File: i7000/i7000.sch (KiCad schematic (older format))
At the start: 53 parts, among them CN01 Conn_02x30_Counter_Clockwise, CN04 Conn_02x30_Counter_Clockwise, CN05 Conn_02x07_Counter_Clockwise

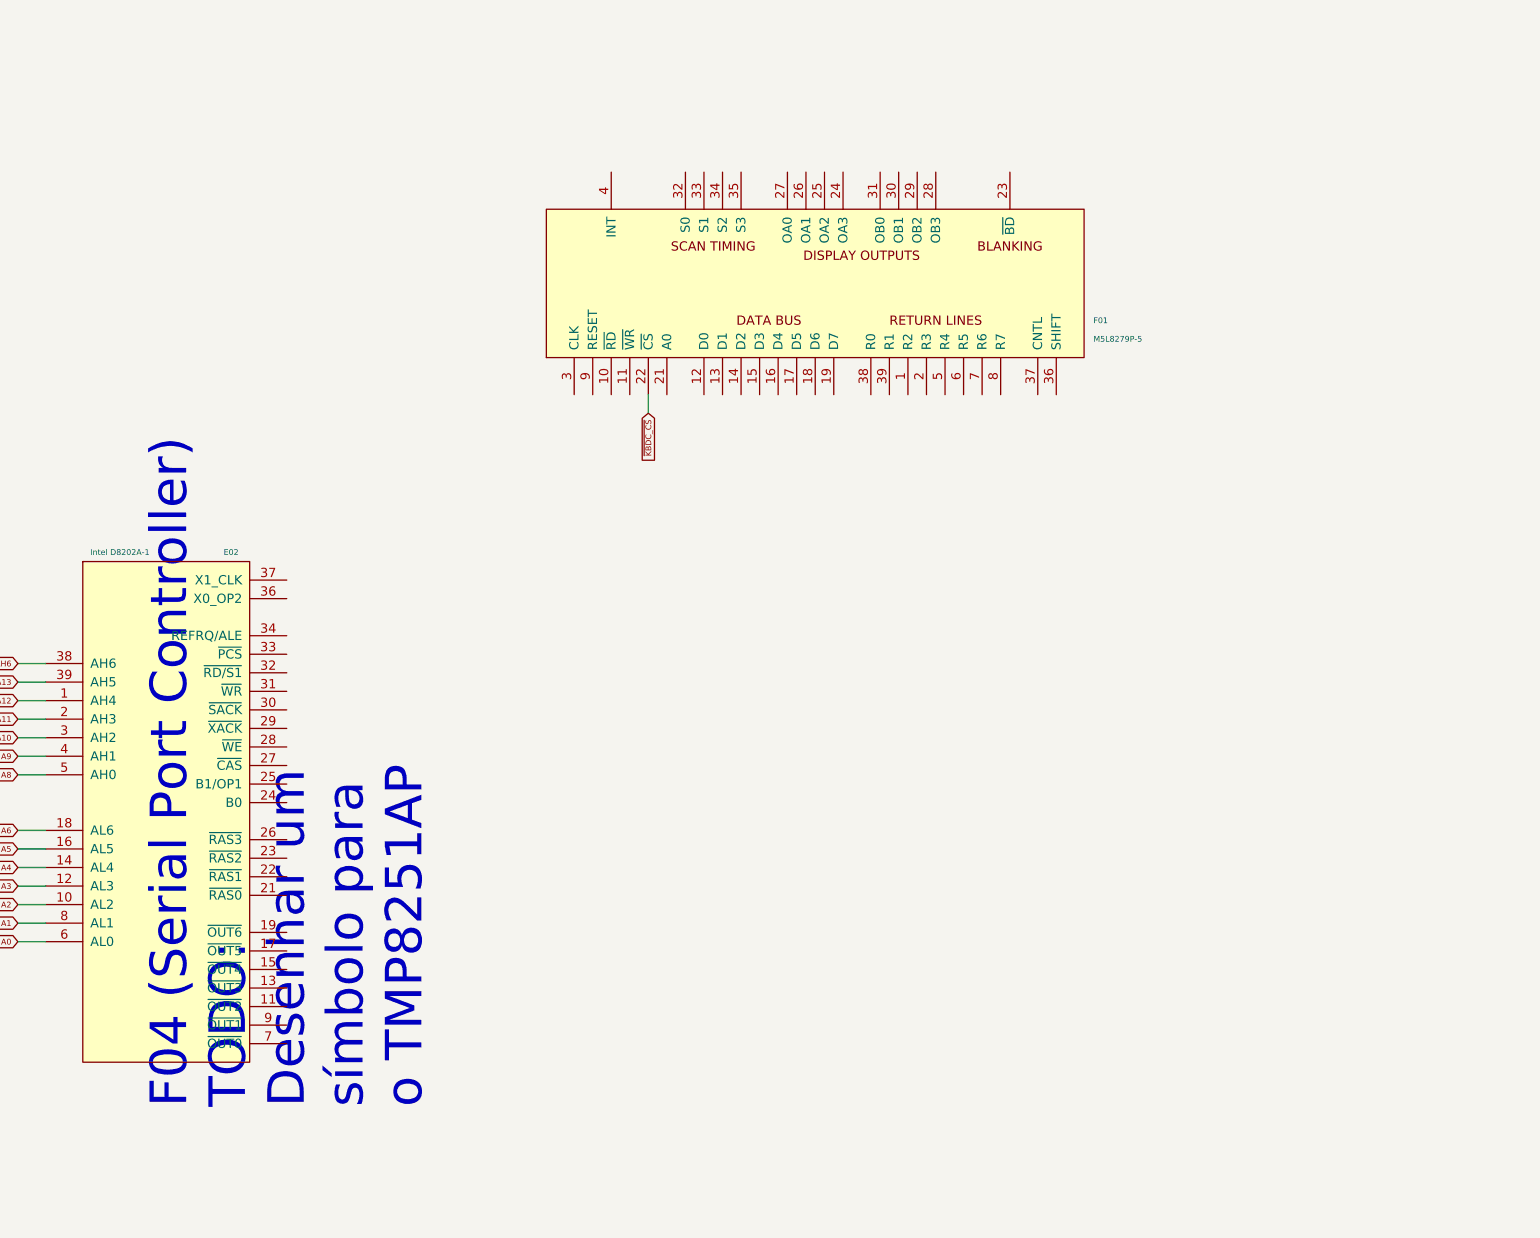
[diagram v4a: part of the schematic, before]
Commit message: TMP8251AP - Programmable Communication Interface (Serial Port Controller)
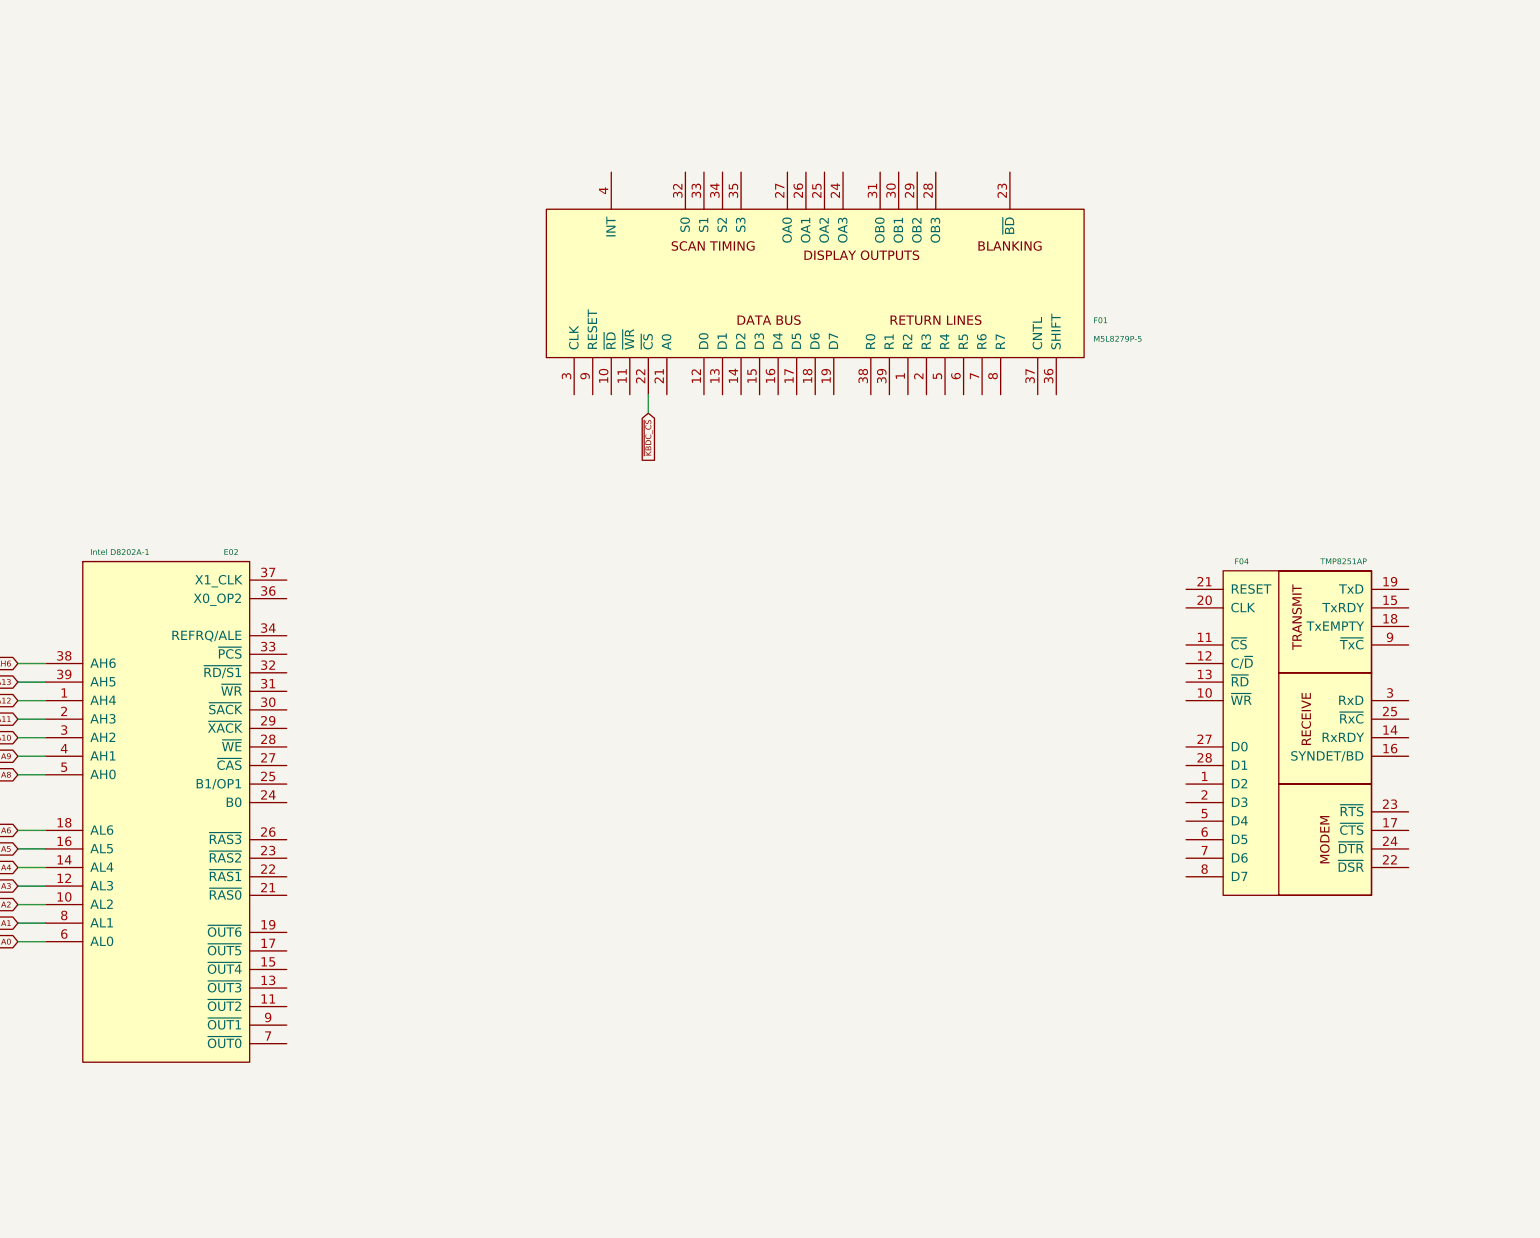
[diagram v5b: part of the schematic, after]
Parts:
- added F04: TMP8251AP, symbol chips_not_yet_available_on_kicad:TMP8251AP
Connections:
- net GND: now also F04.4 (GND)
- net VCC: now also F04.26 (VCC)
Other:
- note removed: "F04 (Serial Port Controller)\nTODO:\nDesenhar um\nsímbolo para\no TMP8251AP"
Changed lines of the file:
@@
 Wire Wire Line
 	25650 5150 25800 5150
-Text Notes 28200 12100 1    197  ~ 0
-F04 (Serial Port Controller)\nTODO:\nDesenhar um\nsímbolo para\no TMP8251AP
 Text GLabel 13600 6250 2    31   Output ~ 0
 ~I8251_CS
@@
 Wire Wire Line
 	29400 8350 29400 8250
+$Comp
+L chips_not_yet_available_on_kicad:TMP8251AP F04
+U 1 1 622E056F
+P 32850 10050
+F 0 "F04" H 32600 10950 31  0000 C CNN
+F 1 "TMP8251AP" H 33150 10950 31  0000 C CNN
+F 2 "" H 33100 10900 31  0001 C CNN
+F 3 "" H 33100 10900 31  0001 C CNN
+	1    32850 10050
+	1    0    0    -1
+$EndComp
 $EndSCHEMATC

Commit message: wip...
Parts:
- added CI03: WD2793A-PL2, symbol chips_not_yet_available_on_kicad:WD2793
- added CI07: 74LS240, symbol Logic_74xx:74LS240
- added CI18: 74LS373, symbol Logic_74xx:74LS373
- added unit 2 of CI19
- added CI20: 74LS14, symbol Logic_74xx:74LS14
- added unit 3 of CI21
- added E07: 74LS245, symbol Logic_74xx:74LS245
- added U?: 8259A, DIP-28, symbol intel:8259A
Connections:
- net A13: now also CI12.2 (A0)
- net A2: now also F07.1 (A0)
- net A3: now also F07.2 (A1)
- net A4: now also F07.3 (A2)
- net CN04_54: now also CN04.54 (Pin_54), E13.7 (O7)
- net GND: now also CI12.3 (A1), CI17.1 (OEa), CI17.10 (GND), CI17.19 (OEb)
- net VCC: now also CI17.20 (VCC)
- net ~FDC_CS: now also CI03.3 (~CS)
- net ~PIC_CS: now reaches F07.10 (O5)
- net ~PIC_CS: now also U?.1 (~CS~)
- net at F07.4 (E1): now also F07.5 (E2)
- net at F07.6 (E3): now also F15.3
- net ~A5: now reaches E28.12, F14.3, F15.2
- net CN04_10: now reaches CN04.10 (Pin_10)
- net CN04_10: now also CN01.10 (Pin_10), E13.14 (O1)
- net IR3: now reaches CN04.25 (Pin_25)
- net IR3: now also CI17.14 (O2a), CN01.25 (Pin_25), U?.21 (IR3)
- net CN04_52: now reaches CN04.52 (Pin_52)
- net CN04_52: now also CN01.52 (Pin_52), E13.13 (O2)
- net CN04_53: now reaches CN04.53 (Pin_53)
- net CN04_53: now also CN01.53 (Pin_53), E13.11 (O4)
- net CN04_07: now reaches CN04.7 (Pin_7)
- net CN04_07: now also CN01.7 (Pin_7), E13.9 (O6)
- net CN04_08: now reaches CN04.8 (Pin_8)
- net CN04_08: now also CN01.8 (Pin_8), E13.10 (O5)
- net CN04_09: now reaches CN04.9 (Pin_9)
- net CN04_09: now also CN01.9 (Pin_9), E13.12 (O3)
- net CI13_CP: now reaches CI13.11 (Cp), CI14.11 (O4)
- net ~CI07_OE: now reaches CI14.9 (O6)
- net ~CI07_OE: now also CI07.1 (OEa), CI07.19 (OEb)
- net FDC_DRQ_2: now reaches CI13.18 (D7)
- net FDC_DRQ_2: now also CI07.3 (O3b), CI18.18 (D7)
- net at CI19.6, CI21.5: now also CI21.9
- net ~CI06_OE: now reaches CI06.1 (OEa), CI21.6
- net ~CI06_OE: now also CI06.19 (OEb)
- net CN04_41: now reaches CN01.41 (Pin_41)
- net CN04_41: now also CI19.3
- net FDC_INTRQ: now reaches CI17.6 (I2a)
- net FDC_INTRQ: now also CI03.39 (INTRQ)
- new net: CI18.11 (LE), CI20.8
- new net: CI19.4, CI21.10
- new net FDC_DRQ: CI03.38 (DRQ), CI07.17 (I3b)
- new net ~CI18_LE: CI20.9, CI21.8
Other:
- note added: "Floppy Controller"
- note added: "READ"
- note added: "WRITE"
- note removed: "CI03 (Floppy Controller)\nTODO:\nDesenhar um\nsímbolo para\no WD2793A-PL2"
- moved on the sheet: CI06, CI09D, CI13, CI14, CI15A, CI16B, CI19C, CI19D, CI19F, CI21B, CI21D, E28F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

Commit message: wip
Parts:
- added E12: 74LS153, symbol Logic_74xx:74LS153
- added unit 2 of E32
- added unit 4 of E32
- added U?: 74LS157, symbol Logic_74xx:74LS157
- E03: renamed from U?; value 8259A -> M5L8259AP
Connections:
- net A14: now also E12.14 (S0)
- net A15: now also E12.2 (S1)
- net CPU_AD0: now also E07.9 (A7)
- net CPU_AD1: now also E07.8 (A6)
- net CPU_AD2: now also E07.7 (A5)
- net CPU_AD3: now also E07.6 (A4)
- net CPU_AD4: now also E07.5 (A3)
- net CPU_AD5: now also E07.4 (A2)
- net CPU_AD6: now also E07.3 (A1)
- net CPU_AD7: now also E07.2 (A0)
- net DRAM_B0: now also E02.24 (B0), E12.7 (Za), E32.12, E32.4
- net GND: now also E02.25 (B1/OP1), E12.1 (Ea), E12.15 (Eb)
- net D7: now reaches CN04.3 (Pin_3)
- net D7: now also E03.4 (D7), E07.18 (B0), E09.18 (D7), E10.18 (D7), E15.19 (O7)
- net D5: now reaches CN04.4 (Pin_4)
- net D5: now also E03.6 (D5), E07.16 (B2), E09.14 (D5), E10.14 (D5), E15.15 (O5)
- net D2: now reaches CN04.5 (Pin_5)
- net D2: now also E03.9 (D2), E07.13 (B5), E09.7 (D2), E10.7 (D2), E15.6 (O2)
- net D3: now reaches CN04.55 (Pin_55)
- net D3: now also E03.8 (D3), E07.14 (B4), E09.8 (D3), E10.8 (D3), E15.9 (O3)
- net D1: now reaches CN04.56 (Pin_56)
- net D1: now also E03.10 (D1), E07.12 (B6), E09.4 (D1), E10.4 (D1), E15.5 (O1)
- net D0: now reaches CN04.57 (Pin_57)
- net D0: now also E03.11 (D0), E07.11 (B7), E09.3 (D0), E10.3 (D0), E15.2 (O0)
- net D6: now reaches CN04.58 (Pin_58)
- net D6: now also E03.5 (D6), E07.17 (B1), E09.17 (D6), E10.17 (D6), E15.16 (O6)
- net D4: now reaches CN04.6 (Pin_6)
- net D4: now also E03.7 (D4), E07.15 (B3), E09.13 (D4), E10.13 (D4), E15.12 (O4)
- net at E09.16 (Q6): now also E12.5 (I1a)
- net at E09.19 (Q7): now also E12.11 (I1b)
- net at E09.6 (Q2): now also E12.6 (I0a)
- net at E09.9 (Q3): now also E12.10 (I0b)
- net at E10.16 (Q6): now also E12.3 (I3a)
- net at E10.19 (Q7): now also E12.13 (I3b)
- net at E10.6 (Q2): now also E12.4 (I2a)
- net at E10.9 (Q3): now also E12.12 (I2b)
- net DRAM_OUT4: now reaches E15.13 (D4)
- net DRAM_OUT5: now reaches E15.14 (D5)
- net DRAM_OUT6: now reaches E15.17 (D6)
- net DRAM_OUT7: now reaches E15.18 (D7)
- net DRAM_OUT0: now reaches E15.3 (D0)
- net DRAM_OUT1: now reaches E15.4 (D1)
- net DRAM_OUT2: now reaches E15.7 (D2)
- net DRAM_OUT3: now reaches E15.8 (D3)
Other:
- moved on the sheet: E01, E03, E05, E06, E07, E15

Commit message: DRAM
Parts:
- added E14: 74LS157, symbol Logic_74xx:74LS157
- added U? (x8): MCM6665A, symbol chips_not_yet_available_on_kicad:MCM6665A
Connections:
- net ~DRAM_WR is gone; now on net ~DRAM_CTRL_WR: E36.6
- net A7: now also E14.3 (I1a)
- net GND: now also U?.16 (GND), U?.16 (GND), U?.16 (GND), U?.16 (GND), U?.16 (GND), U?.16 (GND), U?.16 (GND), U?.16 (GND)
- net VCC: now also U?.8 (VCC), U?.8 (VCC), U?.8 (VCC), U?.8 (VCC), U?.8 (VCC), U?.8 (VCC), U?.8 (VCC), U?.8 (VCC)
- net at E13.6 (E3), E32.10, E36.5: now also E32.13
- net at E02.11 (~OUT2): now also U?.6 (A2), U?.6 (A2), U?.6 (A2), U?.6 (A2), U?.6 (A2), U?.6 (A2), U?.6 (A2), U?.6 (A2)
- net at E02.13 (~OUT3): now also U?.12 (A3), U?.12 (A3), U?.12 (A3), U?.12 (A3), U?.12 (A3), U?.12 (A3), U?.12 (A3), U?.12 (A3)
- net at E02.15 (~OUT4): now also U?.11 (A4), U?.11 (A4), U?.11 (A4), U?.11 (A4), U?.11 (A4), U?.11 (A4), U?.11 (A4), U?.11 (A4)
- net at E02.17 (~OUT5): now also U?.10 (A5), U?.10 (A5), U?.10 (A5), U?.10 (A5), U?.10 (A5), U?.10 (A5), U?.10 (A5), U?.10 (A5)
- net at E02.19 (~OUT6): now also U?.13 (A6), U?.13 (A6), U?.13 (A6), U?.13 (A6), U?.13 (A6), U?.13 (A6), U?.13 (A6), U?.13 (A6)
- net at E02.21 (~RAS0): now also U?.4 (~RAS), U?.4 (~RAS), U?.4 (~RAS), U?.4 (~RAS), U?.4 (~RAS), U?.4 (~RAS), U?.4 (~RAS), U?.4 (~RAS)
- net ~DRAM_CTRL_CAS: now reaches E02.27 (~CAS)
- net ~DRAM_CTRL_CAS: now also E32.5
- net at E02.28 (~WE): now also U?.3 (~W), U?.3 (~W), U?.3 (~W), U?.3 (~W), U?.3 (~W), U?.3 (~W), U?.3 (~W), U?.3 (~W)
- net ~DRAM_CTRL_WR: now reaches E02.31 (~WR)
- net at E02.7 (~OUT0): now also U?.5 (A0), U?.5 (A0), U?.5 (A0), U?.5 (A0), U?.5 (A0), U?.5 (A0), U?.5 (A0), U?.5 (A0)
- net at E02.9 (~OUT1): now also U?.7 (A1), U?.7 (A1), U?.7 (A1), U?.7 (A1), U?.7 (A1), U?.7 (A1), U?.7 (A1), U?.7 (A1)
- net at E32.6: now also E14.10 (I1d), E14.11 (I0d)
- net DRAM_AH6 renamed DRAM_CTRL_AH6
- net DRAM_B0 renamed DRAM_CTRL_B0
- net E13_pin2 renamed E11_pin9_Zb
- net E11_pin9_Zb: now also E14.2 (I0a)
- new net DRAM_A7: E14.4 (Za), U?.9 (A7), U?.9 (A7), U?.9 (A7), U?.9 (A7), U?.9 (A7), U?.9 (A7), U?.9 (A7), U?.9 (A7)
- new net ~DRAM_CAS: E14.9 (Zd), U?.15 (~CAS), U?.15 (~CAS), U?.15 (~CAS), U?.15 (~CAS), U?.15 (~CAS), U?.15 (~CAS), U?.15 (~CAS), U?.15 (~CAS)
- no-connect marks 0 -> 8
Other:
- moved on the sheet: E02, E03, E13, E32A, E32B, E32C, E32D, E36B, F04
